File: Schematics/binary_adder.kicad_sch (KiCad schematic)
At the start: 34 parts, among them J1 Conn_01x02, SW1 SW_Push, SW2 SW_Push, U1 4040, U2 LM555xN

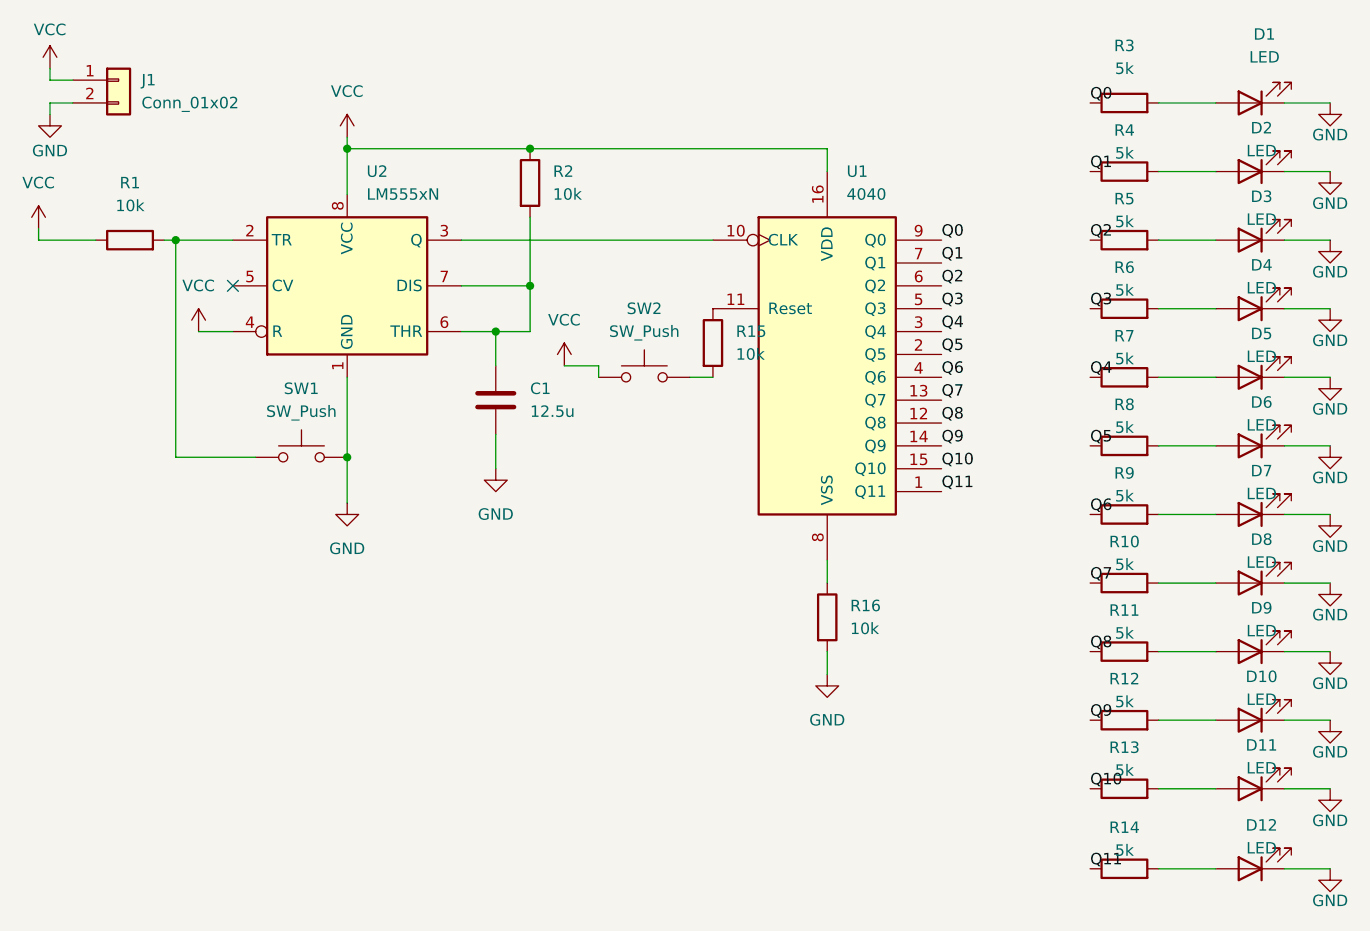
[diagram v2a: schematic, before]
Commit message: Change pull down resistor
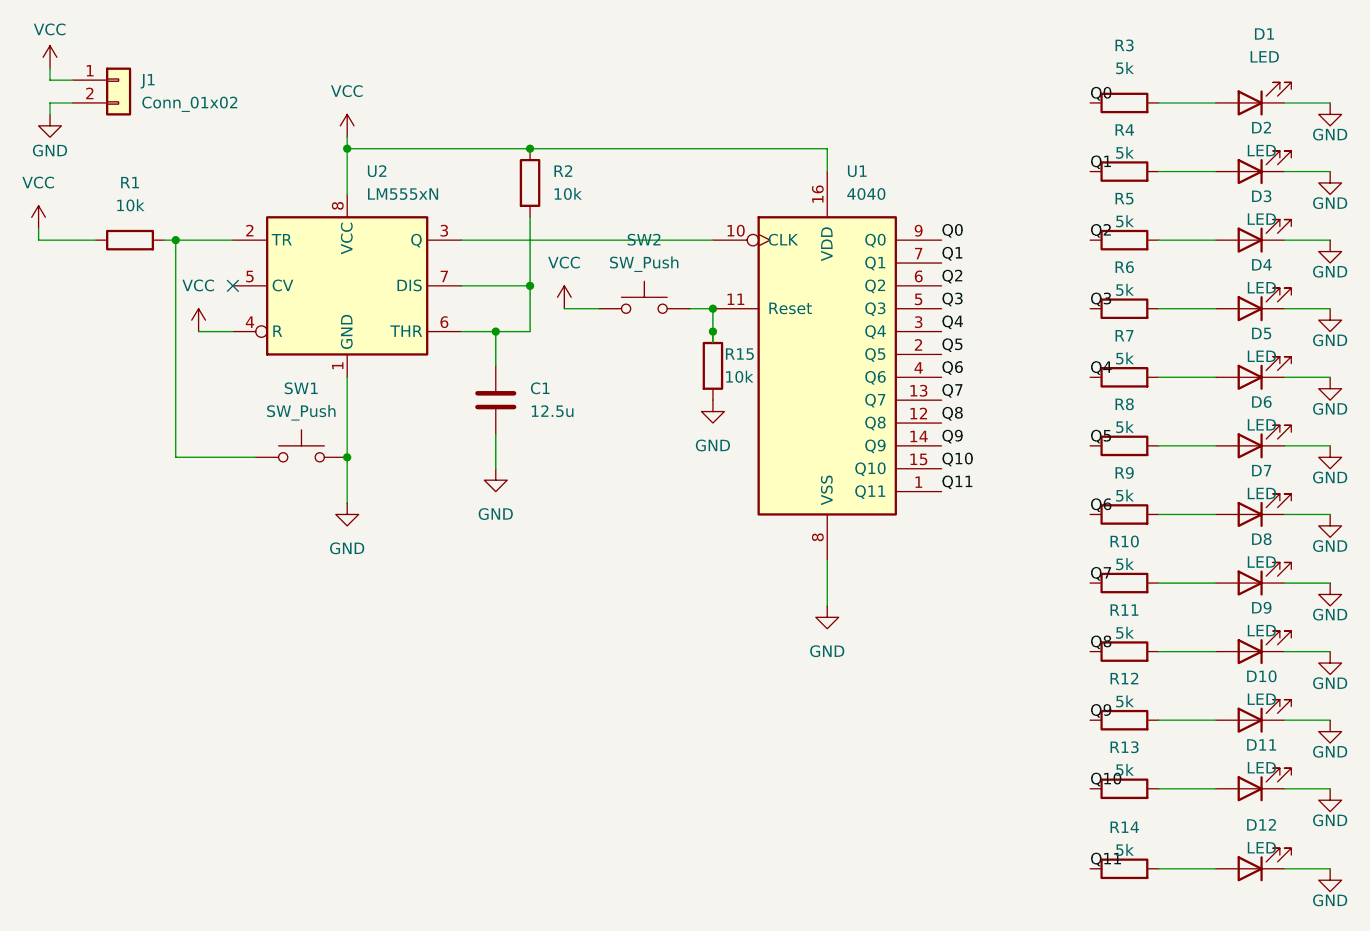
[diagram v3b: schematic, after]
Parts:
- removed R16: 10k, Resistor_THT:R_Axial_DIN0204_L3.6mm_D1.6mm_P7.62mm_Horizontal, symbol Device:R
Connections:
- net GND: now also R15.2, U1.8 (VSS)
- net at R15.1, U1.11 (Reset): now also SW2.2
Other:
- moved on the sheet: R15, SW2
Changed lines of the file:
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@@
 	)
 	(junction
+		(at 96.52 44.45)
+		(diameter 0)
+		(color 0 0 0 0)
+	)
+	(junction
 		(at 76.2 26.67)
 		(diameter 0)
@@
 		(color 0 0 0 0)
 	)
+	(junction
+		(at 96.52 46.99)
+		(diameter 0)
+		(color 0 0 0 0)
+	)
 	(no_connect
 		(at 43.18 41.91)
@@
 	(wire
 		(pts
-			(xy 109.22 82.55) (xy 109.22 85.09)
+			(xy 109.22 72.39) (xy 109.22 77.47)
 		)
 		(stroke
@@
 	(wire
 		(pts
-			(xy 83.82 50.8) (xy 80.01 50.8)
-		)
-		(stroke
-			(width 0)
-			(type default)
-		)
-	)
-	(wire
-		(pts
-			(xy 109.22 72.39) (xy 109.22 74.93)
+			(xy 83.82 44.45) (xy 80.01 44.45)
 		)
 		(stroke
@@
 	(wire
 		(pts
+			(xy 96.52 44.45) (xy 96.52 46.99)
+		)
+		(stroke
+			(width 0)
+			(type default)
+		)
+	)
+	(wire
+		(pts
 			(xy 146.05 29.21) (xy 152.4 29.21)
 		)
@@
 	(wire
 		(pts
-			(xy 55.88 26.67) (xy 76.2 26.67)
+			(xy 96.52 46.99) (xy 96.52 48.26)
 		)
 		(stroke
@@
 	(wire
 		(pts
-			(xy 146.05 59.69) (xy 152.4 59.69)
+			(xy 55.88 26.67) (xy 76.2 26.67)
 		)
 		(stroke
@@
 	(wire
 		(pts
-			(xy 160.02 74.93) (xy 165.1 74.93)
+			(xy 146.05 59.69) (xy 152.4 59.69)
 		)
 		(stroke
@@
 	(wire
 		(pts
-			(xy 55.88 60.96) (xy 55.88 66.04)
+			(xy 160.02 74.93) (xy 165.1 74.93)
 		)
 		(stroke
@@
 	(wire
 		(pts
-			(xy 21.59 35.56) (xy 21.59 36.83)
+			(xy 55.88 60.96) (xy 55.88 66.04)
 		)
 		(stroke
@@
 	(wire
 		(pts
-			(xy 83.82 52.07) (xy 83.82 50.8)
+			(xy 21.59 35.56) (xy 21.59 36.83)
 		)
 		(stroke
@@
 	(wire
 		(pts
-			(xy 146.05 44.45) (xy 152.4 44.45)
+			(xy 93.98 44.45) (xy 96.52 44.45)
 		)
 		(stroke
@@
 	(wire
 		(pts
-			(xy 68.58 36.83) (xy 96.52 36.83)
+			(xy 146.05 44.45) (xy 152.4 44.45)
 		)
 		(stroke
@@
 	(wire
 		(pts
-			(xy 93.98 52.07) (xy 96.52 52.07)
+			(xy 68.58 36.83) (xy 96.52 36.83)
 		)
 		(stroke
@@
 	(symbol
 		(lib_id "power:GND")
+		(at 96.52 54.61 0)
+		(unit 1)
+		(exclude_from_sim no)
+		(in_bom yes)
+		(on_board yes)
+		(dnp no)
+		(fields_autoplaced yes)
+		(property "Reference" "#PWR022"
+			(at 96.52 60.96 0)
+			(effects
+				(font
+					(size 1.27 1.27)
+				)
+				(hide yes)
+			)
+		)
+		(property "Value" "GND"
+			(at 96.52 59.69 0)
+			(effects
+				(font
+					(size 1.27 1.27)
+				)
+			)
+		)
+		(property "Footprint" ""
+			(at 96.52 54.61 0)
+			(effects
+				(font
+					(size 1.27 1.27)
+				)
+				(hide yes)
+			)
+		)
+		(property "Datasheet" ""
+			(at 96.52 54.61 0)
+			(effects
+				(font
+					(size 1.27 1.27)
+				)
+				(hide yes)
+			)
+		)
+		(property "Description" "Power symbol creates a global label with name \"GND\" , ground"
+			(at 96.52 54.61 0)
+			(effects
+				(font
+					(size 1.27 1.27)
+				)
+				(hide yes)
+			)
+		)
+		(pin "1"
+		)
+		(instances
+			(project ""
+				(path "/b3a9ba6c-8330-4a6b-a1ac-bc265156909f"
+					(reference "#PWR022")
+					(unit 1)
+				)
+			)
+		)
+	)
+	(symbol
+		(lib_id "power:GND")
 		(at 22.86 22.86 0)
 		(unit 1)
@@
 	(symbol
 		(lib_id "Device:R")
-		(at 96.52 48.26 0)
+		(at 96.52 50.8 0)
 		(unit 1)
 		(exclude_from_sim no)
@@
 		(on_board yes)
 		(dnp no)
-		(fields_autoplaced yes)
 		(property "Reference" "R15"
-			(at 99.06 46.9899 0)
+			(at 97.79 49.53 0)
 			(effects
 				(font
@@
 		)
 		(property "Value" "10k"
-			(at 99.06 49.5299 0)
+			(at 97.79 52.07 0)
 			(effects
 				(font
@@
 		)
 		(property "Footprint" "Resistor_THT:R_Axial_DIN0204_L3.6mm_D1.6mm_P7.62mm_Horizontal"
-			(at 94.742 48.26 90)
+			(at 94.742 50.8 90)
 			(effects
 				(font
@@
 		)
 		(property "Datasheet" "~"
-			(at 96.52 48.26 0)
+			(at 96.52 50.8 0)
 			(effects
 				(font
@@
 		)
 		(property "Description" "Resistor"
-			(at 96.52 48.26 0)
+			(at 96.52 50.8 0)
 			(effects
 				(font
@@
 	(symbol
 		(lib_id "power:VCC")
-		(at 80.01 50.8 0)
+		(at 80.01 44.45 0)
 		(unit 1)
 		(exclude_from_sim no)
@@
 		(on_board yes)
 		(dnp no)
-		(fields_autoplaced yes)
 		(property "Reference" "#PWR07"
-			(at 80.01 54.61 0)
+			(at 80.01 48.26 0)
 			(effects
 				(font
@@
 		)
 		(property "Value" "VCC"
-			(at 80.01 45.72 0)
+			(at 80.01 39.37 0)
 			(effects
 				(font
@@
 		)
 		(property "Footprint" ""
-			(at 80.01 50.8 0)
+			(at 80.01 44.45 0)
 			(effects
 				(font
@@
 		)
 		(property "Datasheet" ""
-			(at 80.01 50.8 0)
+			(at 80.01 44.45 0)
 			(effects
 				(font
@@
 		)
 		(property "Description" "Power symbol creates a global label with name \"VCC\""
-			(at 80.01 50.8 0)
+			(at 80.01 44.45 0)
 			(effects
 				(font
@@
 	(symbol
 		(lib_id "Switch:SW_Push")
-		(at 88.9 52.07 0)
+		(at 88.9 44.45 0)
 		(unit 1)
 		(exclude_from_sim no)
@@
 		(fields_autoplaced yes)
 		(property "Reference" "SW2"
-			(at 88.9 44.45 0)
+			(at 88.9 36.83 0)
 			(effects
 				(font
@@
 		)
 		(property "Value" "SW_Push"
-			(at 88.9 46.99 0)
+			(at 88.9 39.37 0)
 			(effects
 				(font
@@
 		)
 		(property "Footprint" "Button_Switch_THT:SW_PUSH_6mm"
-			(at 88.9 46.99 0)
+			(at 88.9 39.37 0)
 			(effects
 				(font
@@
 		)
 		(property "Datasheet" "~"
-			(at 88.9 46.99 0)
+			(at 88.9 39.37 0)
 			(effects
 				(font
@@
 		)
 		(property "Description" "Push button switch, generic, two pins"
-			(at 88.9 52.07 0)
+			(at 88.9 44.45 0)
 			(effects
 				(font
@@
 	(symbol
 		(lib_id "Device:R")
-		(at 109.22 78.74 0)
-		(unit 1)
-		(exclude_from_sim no)
-		(in_bom yes)
-		(on_board yes)
-		(dnp no)
-		(fields_autoplaced yes)
-		(property "Reference" "R16"
-			(at 111.76 77.4699 0)
-			(effects
-				(font
-					(size 1.27 1.27)
-				)
-				(justify left)
-			)
-		)
-		(property "Value" "10k"
-			(at 111.76 80.0099 0)
-			(effects
-				(font
-					(size 1.27 1.27)
-				)
-				(justify left)
-			)
-		)
-		(property "Footprint" "Resistor_THT:R_Axial_DIN0204_L3.6mm_D1.6mm_P7.62mm_Horizontal"
-			(at 107.442 78.74 90)
-			(effects
-				(font
-					(size 1.27 1.27)
-				)
-				(hide yes)
-			)
-		)
-		(property "Datasheet" "~"
-			(at 109.22 78.74 0)
-			(effects
-				(font
-					(size 1.27 1.27)
-				)
-				(hide yes)
-			)
-		)
-		(property "Description" "Resistor"
-			(at 109.22 78.74 0)
-			(effects
-				(font
-					(size 1.27 1.27)
-				)
-				(hide yes)
-			)
-		)
-		(pin "1"
-		)
-		(pin "2"
-		)
-		(instances
-			(project ""
-				(path "/b3a9ba6c-8330-4a6b-a1ac-bc265156909f"
-					(reference "R16")
-					(unit 1)
-				)
-			)
-		)
-	)
-	(symbol
-		(lib_id "Device:R")
 		(at 76.2 30.48 0)
 		(unit 1)
@@
 	(symbol
 		(lib_id "power:GND")
-		(at 109.22 85.09 0)
+		(at 109.22 77.47 0)
 		(unit 1)
 		(exclude_from_sim no)
@@
 		(fields_autoplaced yes)
 		(property "Reference" "#PWR06"
-			(at 109.22 91.44 0)
+			(at 109.22 83.82 0)
 			(effects
 				(font
@@
 		)
 		(property "Value" "GND"
-			(at 109.22 90.17 0)
+			(at 109.22 82.55 0)
 			(effects
 				(font
@@
 		)
 		(property "Footprint" ""
-			(at 109.22 85.09 0)
+			(at 109.22 77.47 0)
 			(effects
 				(font
@@
 		)
 		(property "Datasheet" ""
-			(at 109.22 85.09 0)
+			(at 109.22 77.47 0)
 			(effects
 				(font
@@
 		)
 		(property "Description" "Power symbol creates a global label with name \"GND\" , ground"
-			(at 109.22 85.09 0)
+			(at 109.22 77.47 0)
 			(effects
 				(font
